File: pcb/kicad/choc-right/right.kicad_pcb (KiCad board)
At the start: 2 copper layers, 135.9 x 90.2 mm, 61 parts, among them J1 USB_C_Receptacle_USB2.0, J2 AudioJack4, J3 Conn_01x12_Male, SW1 BOOT, SW10 SW_Push, SW12 SW_Push, SW13 SW_Push, SW14 SW_Push, SW15 SW_Push, SW17 SW_Push, SW18 SW_Push, SW19 SW_Push, SW2 RESET, SW21 SW_Push, SW22 SW_Push, SW23 SW_Push, SW24 SW_Push, SW3 SW_Push, SW31 SW_Push, SW32 SW_Push, SW33 SW_Push, SW34 SW_Push, SW4 SW_Push, SW5 SW_Push, SW7 SW_Push, SW8 SW_Push, SW9 SW_Push, U1 STM32, U2 LDO

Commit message: right side.
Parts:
- SW10, SW12, SW13, SW14, SW15, SW17, SW18, SW19, SW21, SW22, SW23, SW24, SW3, SW31, SW32, SW33, SW34, SW4, SW5, SW7, SW8, SW9: footprint custom:CherryMX_Choc_1u -> custom:choc-1
- moved SW15 6.43 mm to (101.1, 130.4)
- moved SW5 6.40 mm to (202.3, 118.7)
- moved SW10 6.32 mm to (158.3, 123.0)
- moved SW24 6.08 mm to (140.2, 123.0)
- moved SW34 6.00 mm to (122.2, 125.6)
- moved SW19 5.66 mm to (184.2, 116.1)
- moved SW4 5.39 mm to (202.3, 101.6)
- moved SW3 5.00 mm to (202.3, 84.6)
- moved SW9 5.00 mm to (166.2, 106.0)
- moved SW18 4.47 mm to (184.2, 99.1)
- moved SW23 4.47 mm to (148.1, 103.4)
- moved SW33 4.12 mm to (130.1, 106.0)
- moved SW14 4.00 mm to (112.0, 108.5)
- moved SW17 4.00 mm to (184.2, 82.0)
- moved SW8 3.61 mm to (166.2, 88.9)
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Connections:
- J1 pad A8: Net-(J1-PadA8) -> (no net)
- J1 pad B8: Net-(J1-PadB8) -> (no net)
- U1 pad 1: VBAT -> (no net)
- U1 pad 10: Net-(U1-Pad10) -> (no net)
- U1 pad 11: Net-(U1-Pad11) -> (no net)
- U1 pad 12: Net-(U1-Pad12) -> (no net)
- U1 pad 13: Net-(U1-Pad13) -> (no net)
- U1 pad 2: Net-(U1-Pad2) -> (no net)
- U1 pad 22: Net-(U1-Pad22) -> (no net)
- U1 pad 26: Net-(U1-Pad26) -> (no net)
- U1 pad 27: Net-(U1-Pad27) -> (no net)
- U1 pad 28: Net-(U1-Pad28) -> (no net)
- U1 pad 29: Net-(U1-Pad29) -> (no net)
- U1 pad 3: Net-(U1-Pad3) -> (no net)
- U1 pad 4: Net-(U1-Pad4) -> (no net)
- U1 pad 5: Net-(U1-Pad5) -> (no net)
- U1 pad 6: Net-(U1-Pad6) -> (no net)
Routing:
- net COL6: track 111.5 -> 98.3 mm
- net Net-(D17-Pad2): track 22.4 -> 12.2 mm
- net COL3: track 167.2 -> 158.7 mm
- net Net-(D24-Pad2): track 87.2 -> 95.5 mm
- net COL1: track 187.5 -> 180.9 mm
- net Net-(D12-Pad2): track 75.9 -> 69.5 mm
- net COL4: track 149.6 -> 143.2 mm
- net Net-(D6-Pad2): track 123.5 -> 129.8 mm
- net Net-(D20-Pad2): track 105.3 -> 110.8 mm
- net Net-(D14-Pad2): track 67.1 -> 61.6 mm
- net Net-(D26-Pad2): track 57.9 -> 52.5 mm
- net COL5: track 131.1 -> 125.7 mm
- net Net-(D19-Pad2): track 118.6 -> 123.7 mm
- net Net-(D36-Pad2): track 39.7 -> 34.7 mm
- net Net-(D21-Pad2): track 99.7 -> 94.8 mm
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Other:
- board size 135.9 x 90.2 mm -> 130.6 x 82 mm

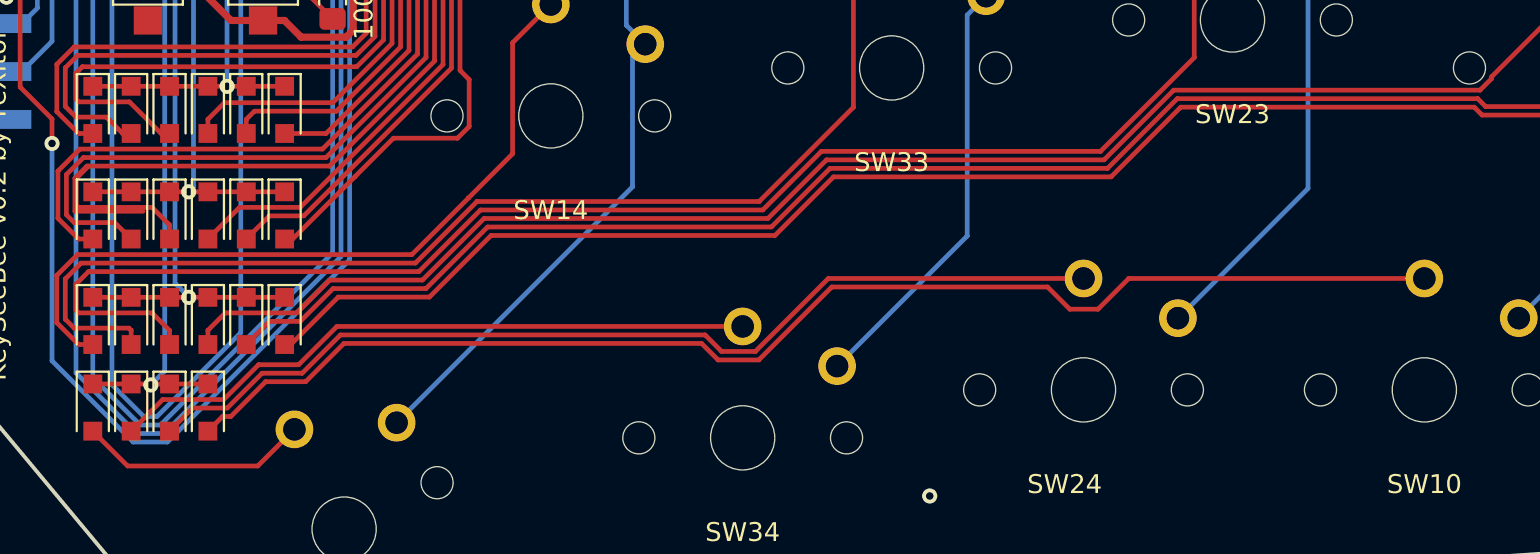
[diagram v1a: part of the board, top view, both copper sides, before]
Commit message: made the right side's routing more similar to the left side's.
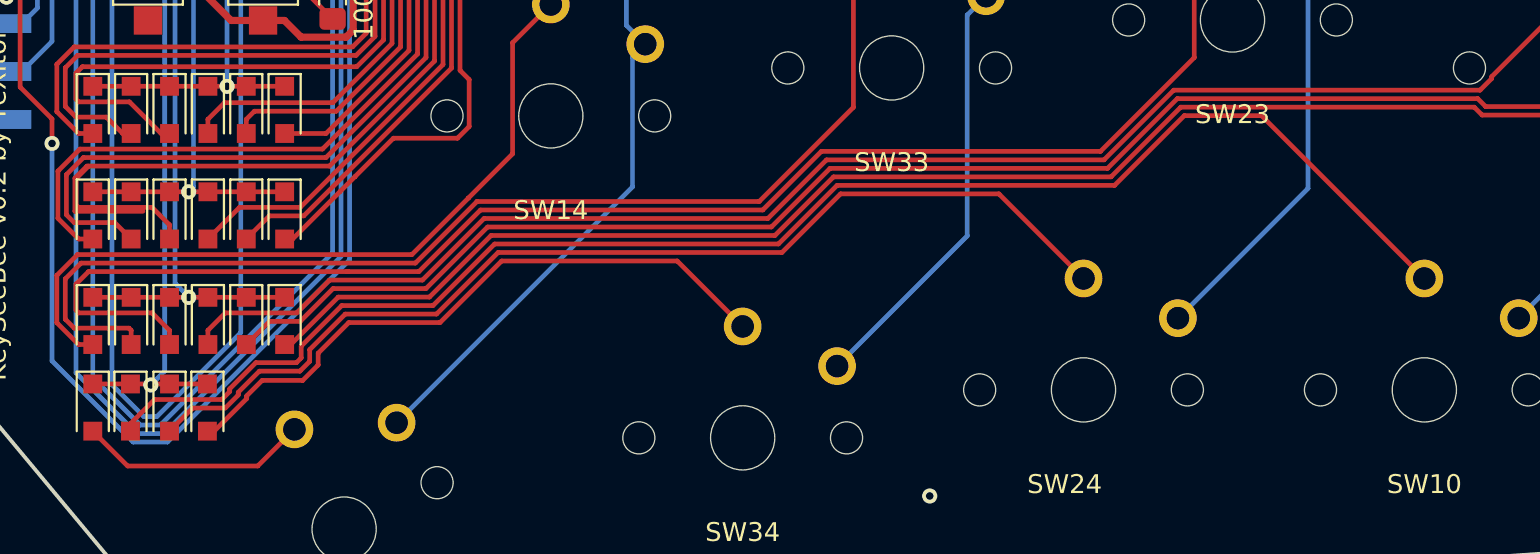
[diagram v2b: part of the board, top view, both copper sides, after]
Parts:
- moved D12 4.10 mm to (89.8, 124.0)
- moved D36 4.04 mm to (93.8, 124.0)
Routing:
- net Net-(D12-Pad2): track 69.5 -> 79.7 mm
- net Net-(D26-Pad2): track 52.5 -> 55.9 mm
- net Net-(D36-Pad2): track 34.7 -> 34.0 mm

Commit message: missed some routes.
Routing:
- net Net-(D21-Pad2): track 94.8 -> 102.0 mm

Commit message: nine mm difference.
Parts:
- moved SW10 1.25 mm to (157.0, 123.0)
- moved SW24 1.21 mm to (139.0, 123.0)
- moved SW34 1.16 mm to (121.0, 125.6)
- moved SW15 1.00 mm to (100.1, 130.4)
- moved D12 0.50 mm to (89.8, 123.5)
- moved D17 0.50 mm to (87.8, 123.5)
- moved D26 0.50 mm to (91.8, 123.5)
- moved D36 0.50 mm to (93.8, 123.5)
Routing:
- net Net-(D17-Pad2): track 12.2 -> 10.7 mm
- net Net-(D12-Pad2): track 79.7 -> 78.8 mm
- net Net-(D26-Pad2): track 55.9 -> 55.2 mm
- net COL3: track 158.7 -> 159.3 mm
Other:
- outline, holes or cut-outs redrawn
